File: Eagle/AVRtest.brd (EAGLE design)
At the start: 20.6 x 22.8 mm, 8 parts, among them IC1 TINY85

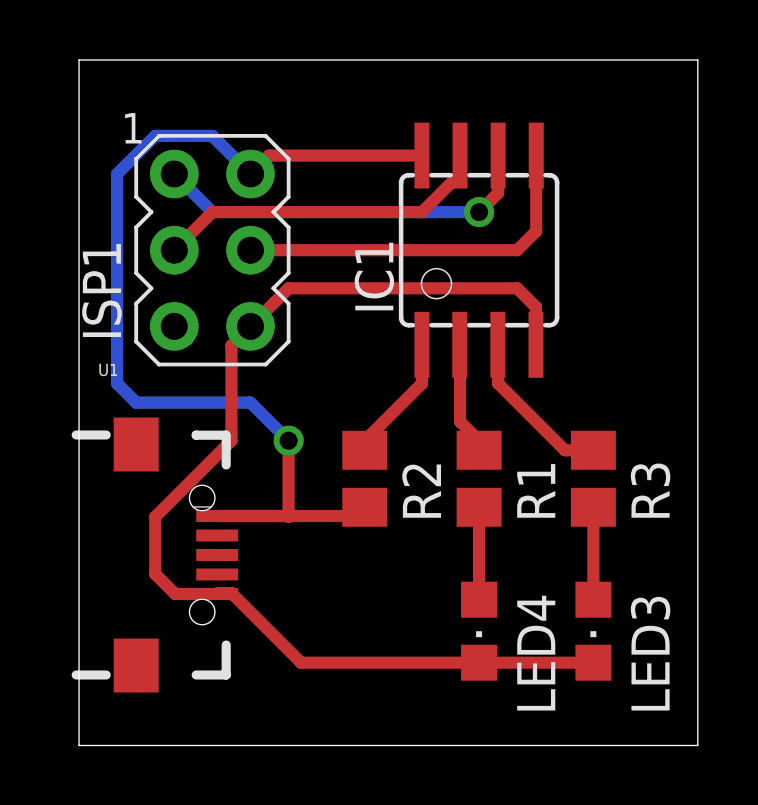
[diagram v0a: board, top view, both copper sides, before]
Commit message: Added ATTINY44 breakout board
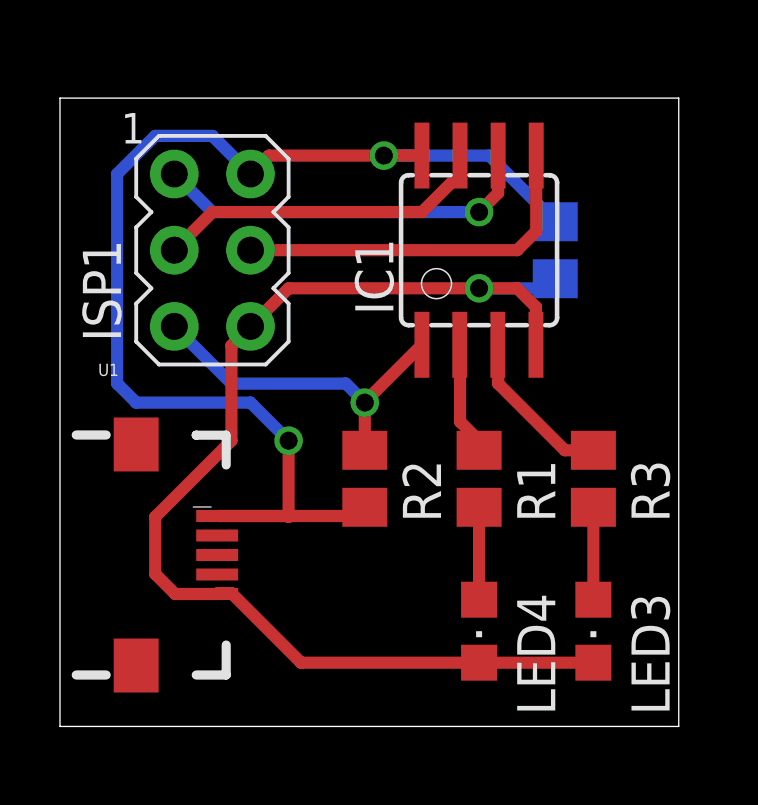
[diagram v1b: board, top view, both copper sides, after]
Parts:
- added C1: (no value), rcl:C0805
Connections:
- net GND: now also C1.2
- net VCC: now also C1.1
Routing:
- net RST: track 4.31 -> 11.7 mm, vias 0 -> 1
- net VCC: track 35.1 -> 41.7 mm, vias 1 -> 2
- net GND: track 37.0 -> 39.7 mm, vias 0 -> 1
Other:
- board size 20.6 x 22.8 mm -> 20.6 x 20.9 mm
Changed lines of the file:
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@@
 <board>
 <plain>
-<wire x1="-0.635" y1="19.05" x2="19.99" y2="19.05" width="0" layer="20"/>
-<wire x1="19.99" y1="19.05" x2="19.99" y2="41.9" width="0" layer="20"/>
-<wire x1="19.99" y1="41.9" x2="-0.635" y2="41.9" width="0" layer="20"/>
-<wire x1="-0.635" y1="41.9" x2="-0.635" y2="19.05" width="0" layer="20"/>
+<wire x1="-1.27" y1="19.685" x2="19.355" y2="19.685" width="0" layer="20"/>
+<wire x1="19.355" y1="19.685" x2="19.355" y2="40.63" width="0" layer="20"/>
+<wire x1="19.355" y1="40.63" x2="-1.27" y2="40.63" width="0" layer="20"/>
+<wire x1="-1.27" y1="40.63" x2="-1.27" y2="19.685" width="0" layer="20"/>
 </plain>
 <attributes>
@@
 </class>
 </classes>
-<designrules name="default">
+<designrules name="LaenPCBOrder">
 <description language="de">&lt;b&gt;EAGLE Design Rules&lt;/b&gt;
 &lt;p&gt;
@@
 Einstellungen hier und speichern die Design Rules unter
 einem neuen Namen ab.</description>
-<description language="en">&lt;b&gt;EAGLE Design Rules&lt;/b&gt;
+<description language="en">&lt;b&gt;Laen's PCB Order Design Rules&lt;/b&gt;
 &lt;p&gt;
-The default Design Rules have been set to cover
-a wide range of applications. Your particular design
-may have different requirements, so please make the
-necessary adjustments and save your customized
-design rules under a new name.</description>
+Please make sure your boards conform to these design rules.</description>
 <param name="layerSetup" value="(1*16)"/>
-<param name="mtCopper" value="0.035mm 0.035mm 0.035mm 0.035mm 0.035mm 0.035mm 0.035mm 0.035mm 0.035mm 0.035mm 0.035mm 0.035mm 0.035mm 0.035mm 0.035mm 0.035mm"/>
-<param name="mtIsolate" value="1.5mm 0.15mm 0.2mm 0.15mm 0.2mm 0.15mm 0.2mm 0.15mm 0.2mm 0.15mm 0.2mm 0.15mm 0.2mm 0.15mm 0.2mm"/>
-<param name="mdWireWire" value="8mil"/>
-<param name="mdWirePad" value="8mil"/>
-<param name="mdWireVia" value="8mil"/>
-<param name="mdPadPad" value="8mil"/>
-<param name="mdPadVia" value="8mil"/>
-<param name="mdViaVia" value="8mil"/>
-<param name="mdSmdPad" value="8mil"/>
-<param name="mdSmdVia" value="8mil"/>
-<param name="mdSmdSmd" value="8mil"/>
+<param name="mtCopper" value="0.0356mm 0.0356mm 0.0356mm 0.0356mm 0.0356mm 0.0356mm 0.0356mm 0.0356mm 0.0356mm 0.0356mm 0.0356mm 0.0356mm 0.0356mm 0.0356mm 0.0356mm 0.0356mm"/>
+<param name="mtIsolate" value="1.5011mm 0.1499mm 0.2007mm 0.1499mm 0.2007mm 0.1499mm 0.2007mm 0.1499mm 0.2007mm 0.1499mm 0.2007mm 0.1499mm 0.2007mm 0.1499mm 0.2007mm"/>
+<param name="mdWireWire" value="6mil"/>
+<param name="mdWirePad" value="6mil"/>
+<param name="mdWireVia" value="6mil"/>
+<param name="mdPadPad" value="6mil"/>
+<param name="mdPadVia" value="6mil"/>
+<param name="mdViaVia" value="6mil"/>
+<param name="mdSmdPad" value="6mil"/>
+<param name="mdSmdVia" value="6mil"/>
+<param name="mdSmdSmd" value="6mil"/>
 <param name="mdViaViaSameLayer" value="8mil"/>
 <param name="mnLayersViaInSmd" value="2"/>
-<param name="mdCopperDimension" value="40mil"/>
-<param name="mdDrill" value="8mil"/>
+<param name="mdCopperDimension" value="15mil"/>
+<param name="mdDrill" value="6mil"/>
 <param name="mdSmdStop" value="0mil"/>
-<param name="msWidth" value="10mil"/>
-<param name="msDrill" value="24mil"/>
-<param name="msMicroVia" value="9.99mm"/>
+<param name="msWidth" value="6mil"/>
+<param name="msDrill" value="13mil"/>
+<param name="msMicroVia" value="13mil"/>
 <param name="msBlindViaRatio" value="0.5"/>
 <param name="rvPadTop" value="0.25"/>
@@
 <param name="rvMicroViaOuter" value="0.25"/>
 <param name="rvMicroViaInner" value="0.25"/>
-<param name="rlMinPadTop" value="10mil"/>
+<param name="rlMinPadTop" value="7mil"/>
 <param name="rlMaxPadTop" value="20mil"/>
-<param name="rlMinPadInner" value="10mil"/>
+<param name="rlMinPadInner" value="7mil"/>
 <param name="rlMaxPadInner" value="20mil"/>
-<param name="rlMinPadBottom" value="10mil"/>
+<param name="rlMinPadBottom" value="7mil"/>
 <param name="rlMaxPadBottom" value="20mil"/>
-<param name="rlMinViaOuter" value="8mil"/>
+<param name="rlMinViaOuter" value="7mil"/>
 <param name="rlMaxViaOuter" value="20mil"/>
-<param name="rlMinViaInner" value="8mil"/>
+<param name="rlMinViaInner" value="7mil"/>
 <param name="rlMaxViaInner" value="20mil"/>
 <param name="rlMinMicroViaOuter" value="4mil"/>
@@
 <param name="mvStopFrame" value="1"/>
 <param name="mvCreamFrame" value="0"/>
-<param name="mlMinStopFrame" value="4mil"/>
-<param name="mlMaxStopFrame" value="4mil"/>
+<param name="mlMinStopFrame" value="3mil"/>
+<param name="mlMaxStopFrame" value="3mil"/>
 <param name="mlMinCreamFrame" value="0mil"/>
 <param name="mlMaxCreamFrame" value="0mil"/>
@@
 <element name="ISP1" library="adafruit" package="AVRISP" value="AVRISP-6" x="3.81" y="35.56"/>
 <element name="R2" library="rcl" package="R0805" value="10K" x="8.89" y="27.94" rot="R270"/>
+<element name="C1" library="rcl" package="C0805" value="" x="15.24" y="35.56" rot="MR270"/>
 </elements>
 <signals>
@@
 <wire x1="8.89" y1="26.7" x2="8.89" y2="26.99" width="0.4064" layer="1"/>
 <wire x1="5.08" y1="38.1" x2="5.694" y2="38.714" width="0.4064" layer="1"/>
-<wire x1="5.694" y1="38.714" x2="10.795" y2="38.714" width="0.4064" layer="1"/>
+<wire x1="5.694" y1="38.714" x2="9.525" y2="38.714" width="0.4064" layer="1"/>
 <wire x1="3.97" y1="26.7" x2="6.32" y2="26.7" width="0.4064" layer="1"/>
 <wire x1="6.32" y1="26.7" x2="6.35" y2="26.67" width="0.4064" layer="1"/>
@@
 <wire x1="1.905" y1="39.37" x2="3.81" y2="39.37" width="0.4064" layer="16"/>
 <wire x1="3.81" y1="39.37" x2="5.08" y2="38.1" width="0.4064" layer="16"/>
+<contactref element="C1" pad="1"/>
+<wire x1="15.24" y1="36.51" x2="13.036" y2="38.714" width="0.4064" layer="16"/>
+<wire x1="13.036" y1="38.714" x2="9.525" y2="38.714" width="0.4064" layer="16"/>
+<via x="9.525" y="38.714" extent="1-16" drill="0.6" shape="square"/>
+<wire x1="9.525" y1="38.714" x2="10.795" y2="38.714" width="0.4064" layer="1"/>
 </signal>
 <signal name="GND">
@@
 <contactref element="LED3" pad="C"/>
 <contactref element="ISP1" pad="6"/>
-<wire x1="5.08" y1="33.02" x2="6.35" y2="34.29" width="0.4064" layer="1"/>
-<wire x1="6.35" y1="34.29" x2="13.97" y2="34.29" width="0.4064" layer="1"/>
-<wire x1="13.97" y1="34.29" x2="14.595" y2="33.665" width="0.4064" layer="1"/>
-<wire x1="14.595" y1="33.665" x2="14.595" y2="32.406" width="0.4064" layer="1"/>
 <wire x1="3.97" y1="24.1" x2="2.57" y2="24.1" width="0.4064" layer="1"/>
 <wire x1="2.57" y1="24.1" x2="1.905" y2="24.765" width="0.4064" layer="1"/>
@@
 <wire x1="4.445" y1="24.13" x2="4" y2="24.13" width="0.4064" layer="1"/>
 <wire x1="4" y1="24.13" x2="3.97" y2="24.1" width="0.4064" layer="1"/>
+<contactref element="C1" pad="2"/>
+<wire x1="5.08" y1="33.02" x2="6.35" y2="34.29" width="0.4064" layer="1"/>
+<wire x1="6.35" y1="34.29" x2="12.7" y2="34.29" width="0.4064" layer="1"/>
+<wire x1="14.595" y1="33.665" x2="14.595" y2="32.406" width="0.4064" layer="1"/>
+<wire x1="15.24" y1="34.61" x2="14.92" y2="34.29" width="0.4064" layer="16"/>
+<wire x1="14.92" y1="34.29" x2="12.7" y2="34.29" width="0.4064" layer="16"/>
+<via x="12.7" y="34.29" extent="1-16" drill="0.6"/>
+<wire x1="12.7" y1="34.29" x2="13.97" y2="34.29" width="0.4064" layer="1"/>
+<wire x1="13.97" y1="34.29" x2="14.595" y2="33.665" width="0.4064" layer="1"/>
 </signal>
 <signal name="N$1">
@@
 <contactref element="IC1" pad="1"/>
 <contactref element="R2" pad="1"/>
-<wire x1="8.89" y1="28.89" x2="8.89" y2="29.21" width="0.4064" layer="1"/>
-<wire x1="8.89" y1="29.21" x2="10.795" y2="31.115" width="0.4064" layer="1"/>
-<wire x1="10.795" y1="31.115" x2="10.795" y2="32.406" width="0.4064" layer="1"/>
-<wire x1="8.89" y1="29.21" x2="2.54" y2="33.02" width="0" layer="19" extent="1-1"/>
+<wire x1="2.54" y1="33.02" x2="4.445" y2="31.115" width="0.4064" layer="16"/>
+<wire x1="10.795" y1="32.406" x2="8.89" y2="30.501" width="0.4064" layer="1"/>
+<wire x1="8.89" y1="30.501" x2="8.89" y2="30.48" width="0.4064" layer="1"/>
+<wire x1="8.89" y1="28.89" x2="8.89" y2="30.48" width="0.4064" layer="1"/>
+<via x="8.89" y="30.48" extent="1-16" drill="0.6"/>
+<wire x1="8.89" y1="30.48" x2="8.255" y2="31.115" width="0.4064" layer="16"/>
+<wire x1="8.255" y1="31.115" x2="4.445" y2="31.115" width="0.4064" layer="16"/>
 </signal>
 <signal name="SCK">
@@
 </signal>
 </signals>
+<errors>
+</errors>
 </board>
 </drawing>
